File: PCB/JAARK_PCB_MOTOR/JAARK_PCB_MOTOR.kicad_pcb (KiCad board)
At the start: 2 copper layers, 90 x 90 mm, 55 parts, among them IC1 TPS564242DRLR, IC10 DRV8231DDAR, IC2 PJA3404_R1_00001, IC3 PJA3404_R1_00001, IC4 HIP4080AIBZT, IC5 PJA3404_R1_00001, IC6 PJA3404_R1_00001, IC7 PJA3404_R1_00001, IC8 PJA3404_R1_00001, IC9 DRV8231DDAR, J1 Battery Terminal, Q1 SSM3J334RLF, Q2 SSM3J334RLF, Q3 FMMT619TA, Q4 FMMT619TA, Q5 FMMT619TA, Q6 SSM3J334RLF, Q7 FMMT619TA

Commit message: PCB Motor V1 finished.
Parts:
- removed C8: 22uF, JAARK_lib:CAPC2012X95N
- removed D10, D11, D8, D9: S2JTR, Diode_SMD:D_SMB
- removed IC2, IC3, IC5, IC6, IC7, IC8: PJA3404_R1_00001, JAARK_lib:SOT95P240X110-3N
- removed IC3: PJA3404_R1_00001, SSys_Footprints:SOT95P240X110-3N
- removed IC4: HIP4080AIBZT, JAARK_lib:SOIC127P1032X265-20N
- removed J3, J4: ~, JAARK_lib:1984617
- removed Q2, Q6: SSM3J334RLF, JAARK_lib:2SC2712GRLF
- removed Q3, Q4, Q5, Q7: FMMT619TA, JAARK_lib:SOT95P237X112-3N
- removed R14, R16, R21, R22: 260R, JAARK_lib:RESC2012X60N
- removed R15, R17, R18, R7: 5kR, JAARK_lib:RESC2012X50N
- removed R19, R20: 10kR, JAARK_lib:RESC2012X60N
- added C7: 100uF, JAARK_lib:CAPAE660X800N, F.Cu at (106.9, 124.9)
- added J2: Morpho_x2_SSW-119-01-T-D, JAARK_lib:STM_Nucleo_Morpho_x2_Footprint, F.Cu at (122.5, 122.0)
- added R10: 0.2R, JAARK_lib:RESC2013X65N, B.Cu at (184.1, 115.3)
- added R11: 0.2R, JAARK_lib:RESC2013X65N, B.Cu at (183.7, 62.2)
- added U1: 4A, JAARK_lib:3586TR, F.Cu at (106.7, 60.8)
- C12, C13, C14, C15, IC10, IC9: moved to B.Cu
- D4: footprint Diode_SMD:D_SOD-923 -> JAARK_lib:SODFL3616X135N
- moved J5 147.8 mm to (182.4, 126.0)
- moved J6 138.5 mm to (185.3, 53.2), turned to 180 degrees
- moved IC10 136.3 mm to (174.5, 71.5)
- moved IC9 134.3 mm to (175.0, 107.5)
- moved C13 129.3 mm to (177.6, 98.7), turned to 180 degrees
- moved C15 124.4 mm to (171.7, 81.3)
- moved C14 123.2 mm to (176.9, 101.8)
- moved C12 119.3 mm to (172.2, 78.3), turned to 180 degrees
- moved R2 81.6 mm to (149.8, 107.8), turned to 90 degrees
- moved C3 80.3 mm to (129.2, 103.8), turned to 180 degrees
- moved C1 78.0 mm to (125.7, 107.5), turned to 90 degrees
- moved C5 77.4 mm to (130.3, 107.5), turned to -90 degrees
- moved C4 76.6 mm to (128.0, 107.5), turned to -90 degrees
- moved IC1 72.6 mm to (140.2, 107.5)
- moved R4 68.9 mm to (140.1, 102.5)
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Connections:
- IC10 pad 2: /IN1 -> /IN3
- IC10 pad 3: /IN2 -> /IN4
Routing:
- net +5V: track 0.00 -> 36.0 mm
- net Net-(IC9-OUT1): track 0.00 -> 24.1 mm
- net Net-(IC10-OUT1): track 0.00 -> 21.0 mm
- net GND: track 0.00 -> 19.7 mm, vias 0 -> 15
- net Net-(IC9-OUT2): track 0.00 -> 19.3 mm
- net /IN2: track 0.00 -> 16.3 mm
- net /IN3: track 0.00 -> 13.9 mm, vias 0 -> 1
- net /IN1: track 0.00 -> 13.8 mm
- net Net-(IC10-ISEN): track 0.00 -> 13.5 mm
- net +12V: track 0.00 -> 13.0 mm, vias 0 -> 3
- net /IN4: track 0.00 -> 12.9 mm
- net Net-(IC9-ISEN): track 0.00 -> 9.91 mm
- net Net-(IC1-FB): track 0.00 -> 8.70 mm
- net Net-(J1-Pad2): track 0.00 -> 6.94 mm
- net Net-(IC1-EN): track 0.00 -> 6.83 mm, vias 0 -> 2
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- added copper zone on F.Cu, net +12V
- added copper zone on B.Cu, net +3V3
- added copper zone on B.Cu, net GND
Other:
- board text added: "+"
- board text added: "-"

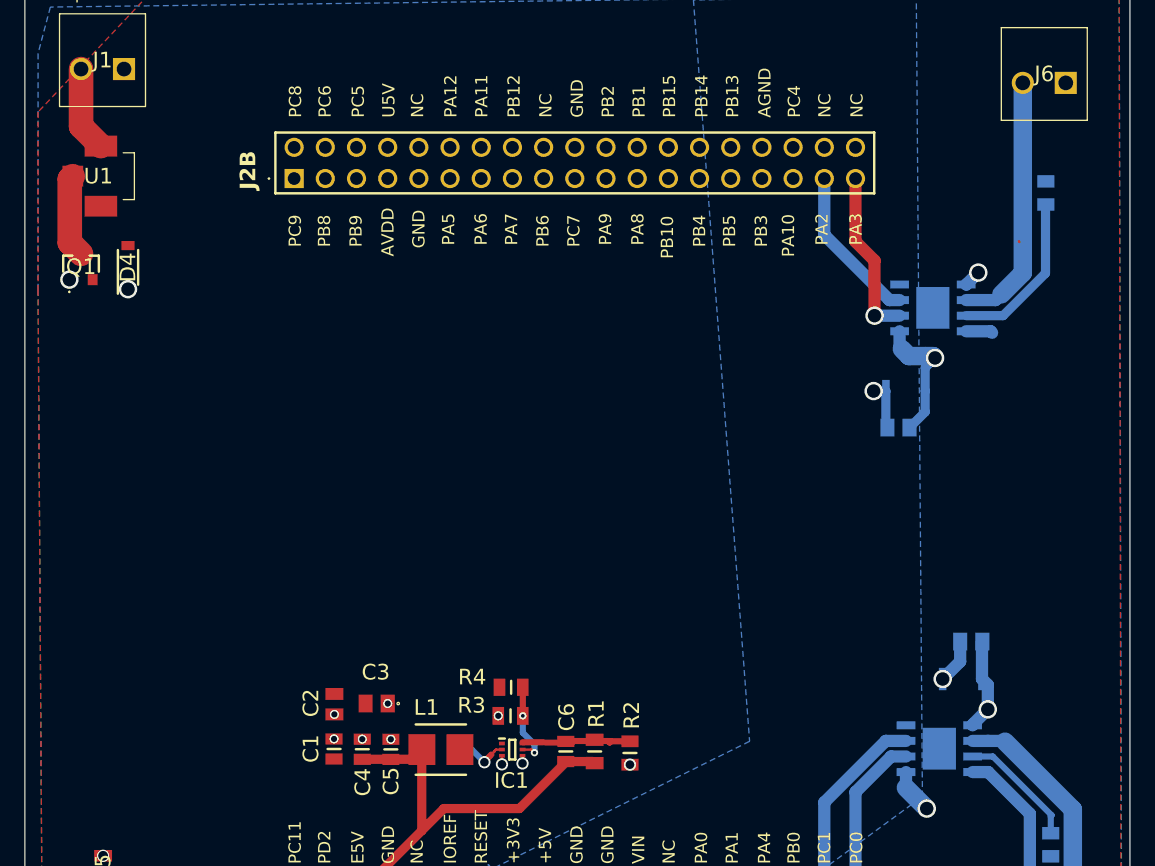
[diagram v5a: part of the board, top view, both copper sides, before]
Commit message: Added mounting holes to Motor PCB, fixed up trace errors
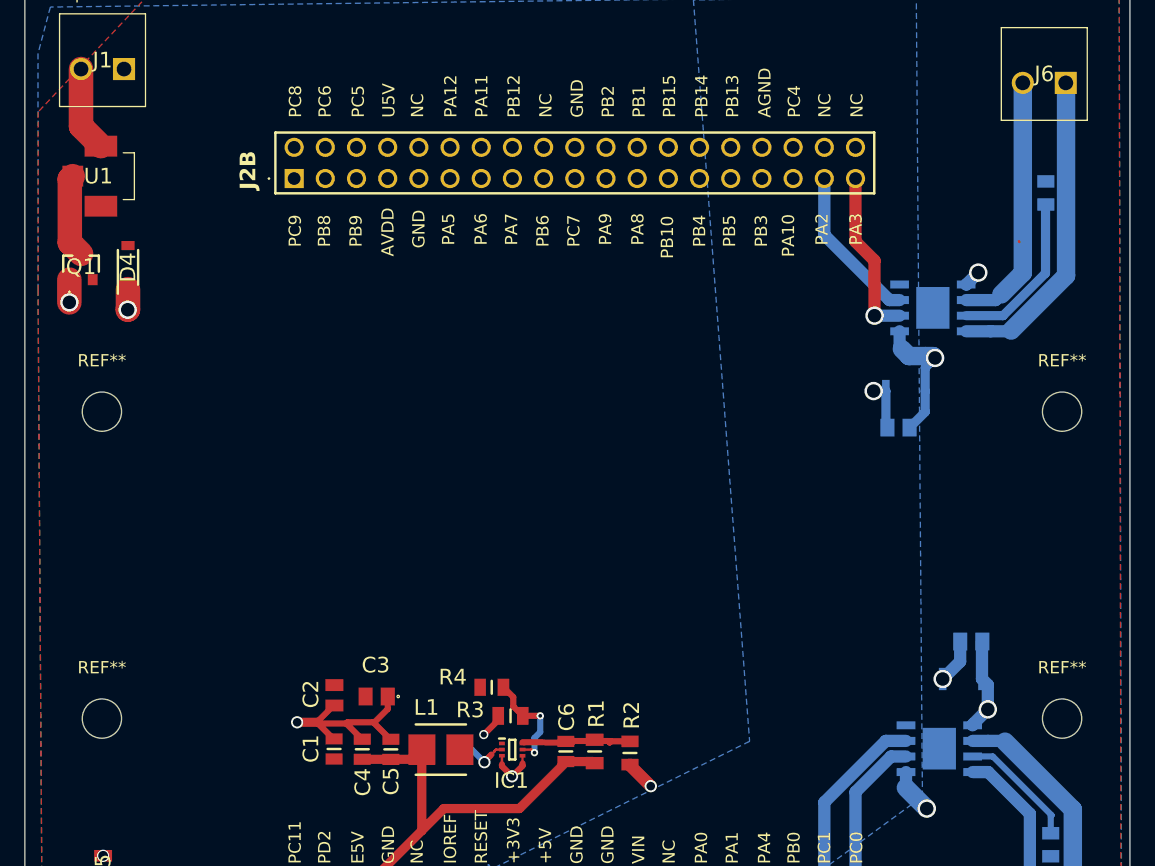
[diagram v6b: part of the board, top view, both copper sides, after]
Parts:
- added REF**: MountingHole_3.2mm_M3, MountingHole:MountingHole_3.2mm_M3, F.Cu at (185.0, 80.0)
- added REF**: MountingHole_3.2mm_M3, MountingHole:MountingHole_3.2mm_M3, F.Cu at (185.0, 105.0)
- added REF**: MountingHole_3.2mm_M3, MountingHole:MountingHole_3.2mm_M3, F.Cu at (106.8, 105.0)
- added REF**: MountingHole_3.2mm_M3, MountingHole:MountingHole_3.2mm_M3, F.Cu at (106.8, 80.0)
- moved R4 1.58 mm to (138.6, 102.5)
- moved C2 0.73 mm to (125.7, 103.1)
- moved C3 0.58 mm to (129.2, 103.2)
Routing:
- net GND: track 19.7 -> 47.1 mm, vias 15 -> 10
- net Net-(IC10-OUT2): track 2.24 -> 25.8 mm
- net Net-(IC1-EN): track 6.83 -> 8.68 mm
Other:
- board text added: "25mm"
- board text added: "78.1mm"

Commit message: forgot one thing
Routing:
- net GND: track 47.1 -> 48.6 mm
- net +12V: track 13.0 -> 13.5 mm
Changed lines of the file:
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@@
 	)
 	(via
-		(at 175.275 101.775)
+		(at 173.8 101.8)
 		(size 1.5)
 		(drill 1.1)
@@
 	)
 	(segment
+		(start 175.275 101.775)
+		(end 173.825 101.775)
+		(width 1)
+		(layer "B.Cu")
+		(net 1)
+	)
+	(segment
 		(start 171.95 74.9)
 		(end 172.525 75.475)
@@
 	)
 	(segment
+		(start 173.825 101.775)
+		(end 173.8 101.8)
+		(width 1)
+		(layer "B.Cu")
+		(net 1)
+	)
+	(segment
 		(start 173.875 75.475)
 		(end 174.5 75.475)
@@
 	)
 	(via
-		(at 169.65 78.325)
-		(size 1.5)
-		(drill 1.1)
-		(layers "F.Cu" "B.Cu")
-		(net 2)
-	)
-	(segment
-		(start 170.65 78.325)
-		(end 169.65 78.325)
-		(width 0.75)
-		(layer "B.Cu")
+		(at 169.1 78.3)
+		(size 1.5)
+		(drill 1.1)
+		(layers "F.Cu" "B.Cu")
 		(net 2)
 	)
@@
 	)
 	(segment
+		(start 170.65 78.325)
+		(end 169.125 78.325)
+		(width 1)
+		(layer "B.Cu")
+		(net 2)
+	)
+	(segment
 		(start 178.475 101.775)
 		(end 178.475 98.75)
@@
 		(width 1)
 		(layer "B.Cu")
+		(net 2)
+	)
+	(segment
+		(start 169.125 78.325)
+		(end 169.1 78.3)
+		(width 1)
+		(layer "B.Cu")

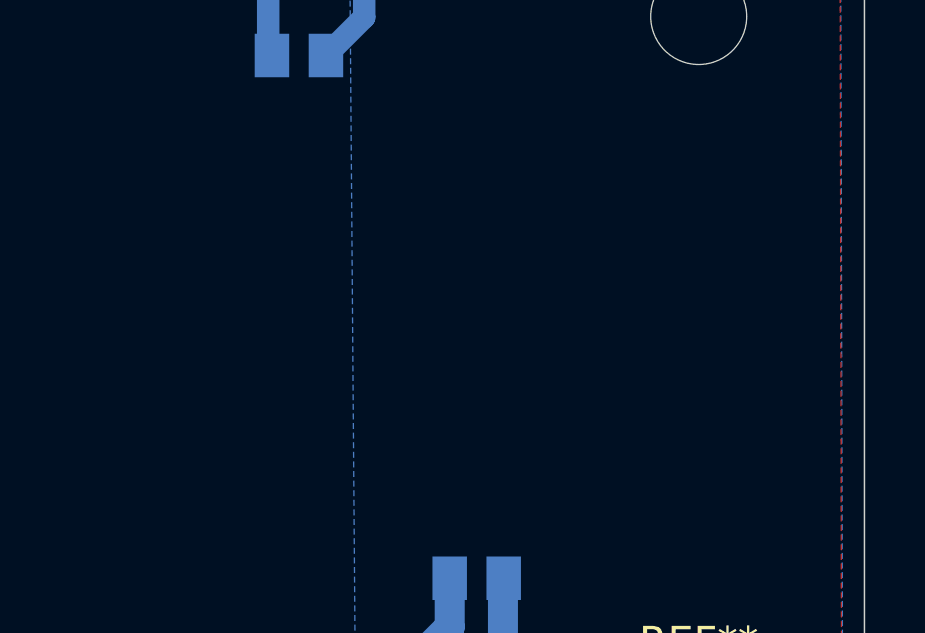
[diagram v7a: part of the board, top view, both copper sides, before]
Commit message: Added heat sink to PCB file and adjusted footprint
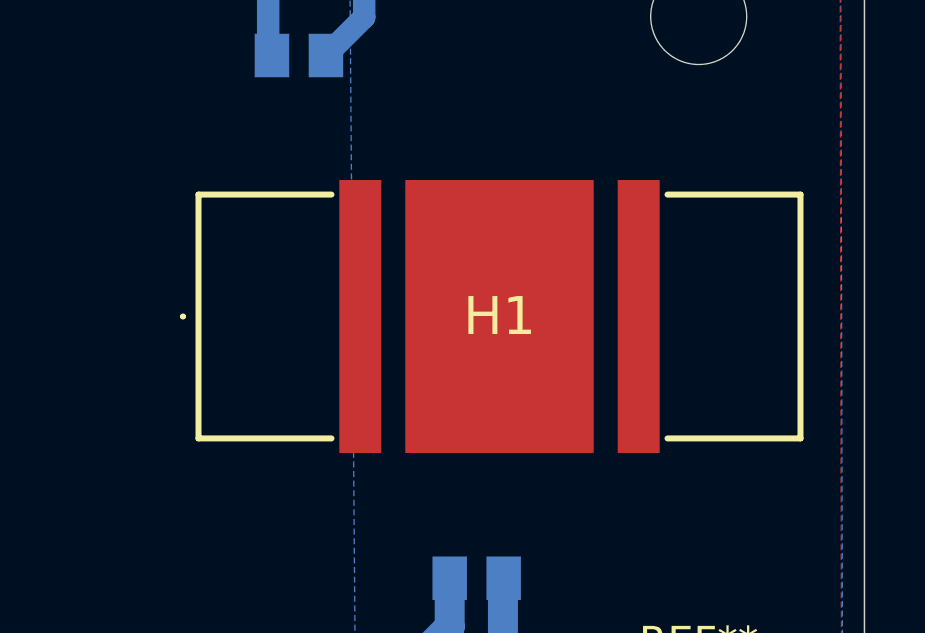
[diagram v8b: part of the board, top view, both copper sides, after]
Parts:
- added H1: V-1100-SMD_B-L, JAARK_lib:V1100SMDBL, F.Cu at (178.4, 90.0)
